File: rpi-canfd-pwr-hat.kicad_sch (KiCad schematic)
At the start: 72 parts, among them J1 Raspberry_Pi, J2 Conn_01x02, J3 Conn_01x02, J5 Conn_01x04_Pin, J6 Conn_01x02, U1 CAT24C256, U12 XC6206P332MR, U13 XC6206P182MR, U2 LM73100, U3 MCP2518FD, U4 TPS259472A, U5 TPS56637, U6 TCAN3413, U7 ICM-20948, Y1 48M

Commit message: schem: assign missing footprints
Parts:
- JP1: footprint (none) -> Jumper:SolderJumper-2_P1.3mm_Open_RoundedPad1.0x1.5mm
- JP2: footprint Jumper:SolderJumper-2_P1.3mm_Open_RoundedPad1.0x1.5mm -> Connector_PinHeader_2.54mm:PinHeader_1x02_P2.54mm_Horizontal
- U1: footprint (none) -> Package_SO:SOIC-8_3.9x4.9mm_P1.27mm
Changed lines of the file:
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@@
 			)
 		)
-		(property "Footprint" ""
+		(property "Footprint" "Jumper:SolderJumper-2_P1.3mm_Open_RoundedPad1.0x1.5mm"
 			(at 165.1 185.42 0)
 			(hide yes)
@@
 			)
 		)
-		(property "Footprint" "Jumper:SolderJumper-2_P1.3mm_Open_RoundedPad1.0x1.5mm"
+		(property "Footprint" "Connector_PinHeader_2.54mm:PinHeader_1x02_P2.54mm_Horizontal"
 			(at 266.7 127 0)
 			(hide yes)
@@
 			)
 		)
-		(property "Footprint" ""
+		(property "Footprint" "Package_SO:SOIC-8_3.9x4.9mm_P1.27mm"
 			(at 151.13 182.88 0)
 			(hide yes)

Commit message: schem: add ordering info to BOM
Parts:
- J1, J2, J3, J6, JP1, TP5, TP7, TP8: now left out of the parts list
- U1: Basic (none) -> X; JLCPCB Part # (none) -> C79987; Manufacturer (none) -> onsemi; Manufacturer Part Number (none) -> CAT24C256WI-GT3
- U12: Basic (none) -> Y; JLCPCB Part # (none) -> C5446; Manufacturer (none) -> Torex Semicon; Manufacturer Part Number (none) -> XC6206P332MR-G
- U13: Basic (none) -> X; JLCPCB Part # (none) -> C347373; Manufacturer (none) -> UMW; Manufacturer Part Number (none) -> XC6206P182MR
- U2: Basic (none) -> X; JLCPCB Part # (none) -> C3210761; Manufacturer (none) -> Texas Instruments; Manufacturer Part Number (none) -> LM73100RPWR
- U3: Basic (none) -> X; JLCPCB Part # (none) -> C621395; Manufacturer (none) -> Microchip Tech; Manufacturer Part Number (none) -> MCP2518FDT-E/QBB
- U6: Basic (none) -> X; JLCPCB Part # (none) -> C22433320; Manufacturer (none) -> Texas Instruments; Manufacturer Part Number (none) -> TCAN3413DR
- U7: Basic (none) -> X; JLCPCB Part # (none) -> C726001; Manufacturer (none) -> TDK InvenSense; Manufacturer Part Number (none) -> ICM-20948

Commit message: schem: add title
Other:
- company: (none) -> Rémi Ait-Younes
- title: (none) -> RPI CAN FD Power Hat+
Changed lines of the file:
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@@
 	(generator_version "10.0")
 	(paper "A4")
+	(title_block
+		(title "RPI CAN FD Power Hat+")
+		(date "2026-04-11")
+		(rev "01")
+		(company "Rémi Ait-Younes")
+	)
 	(rectangle
 		(start 191.77 25.4)

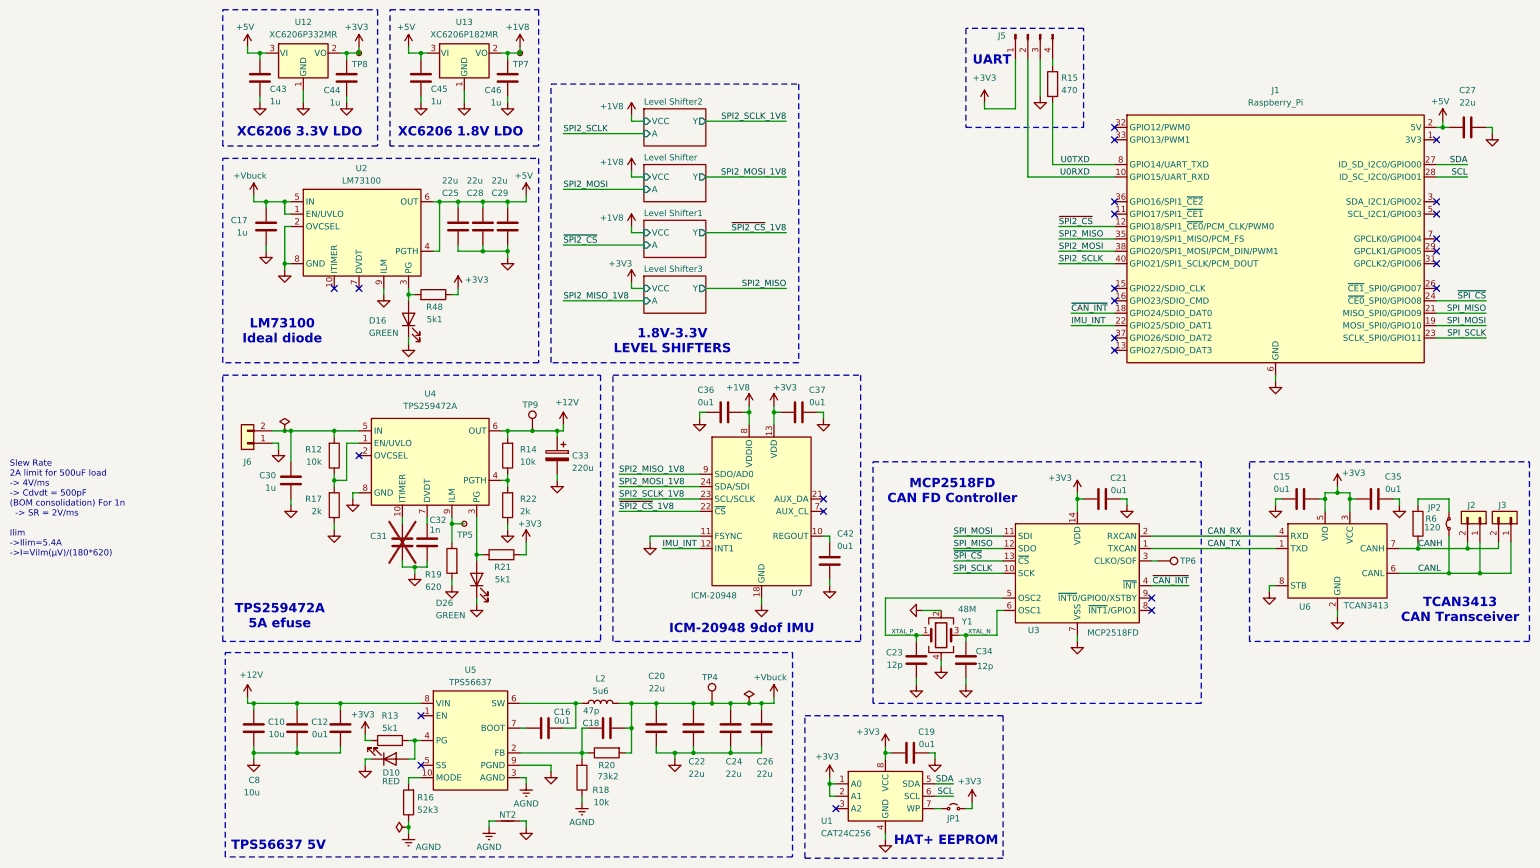
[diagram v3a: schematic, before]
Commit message: schem: renumber
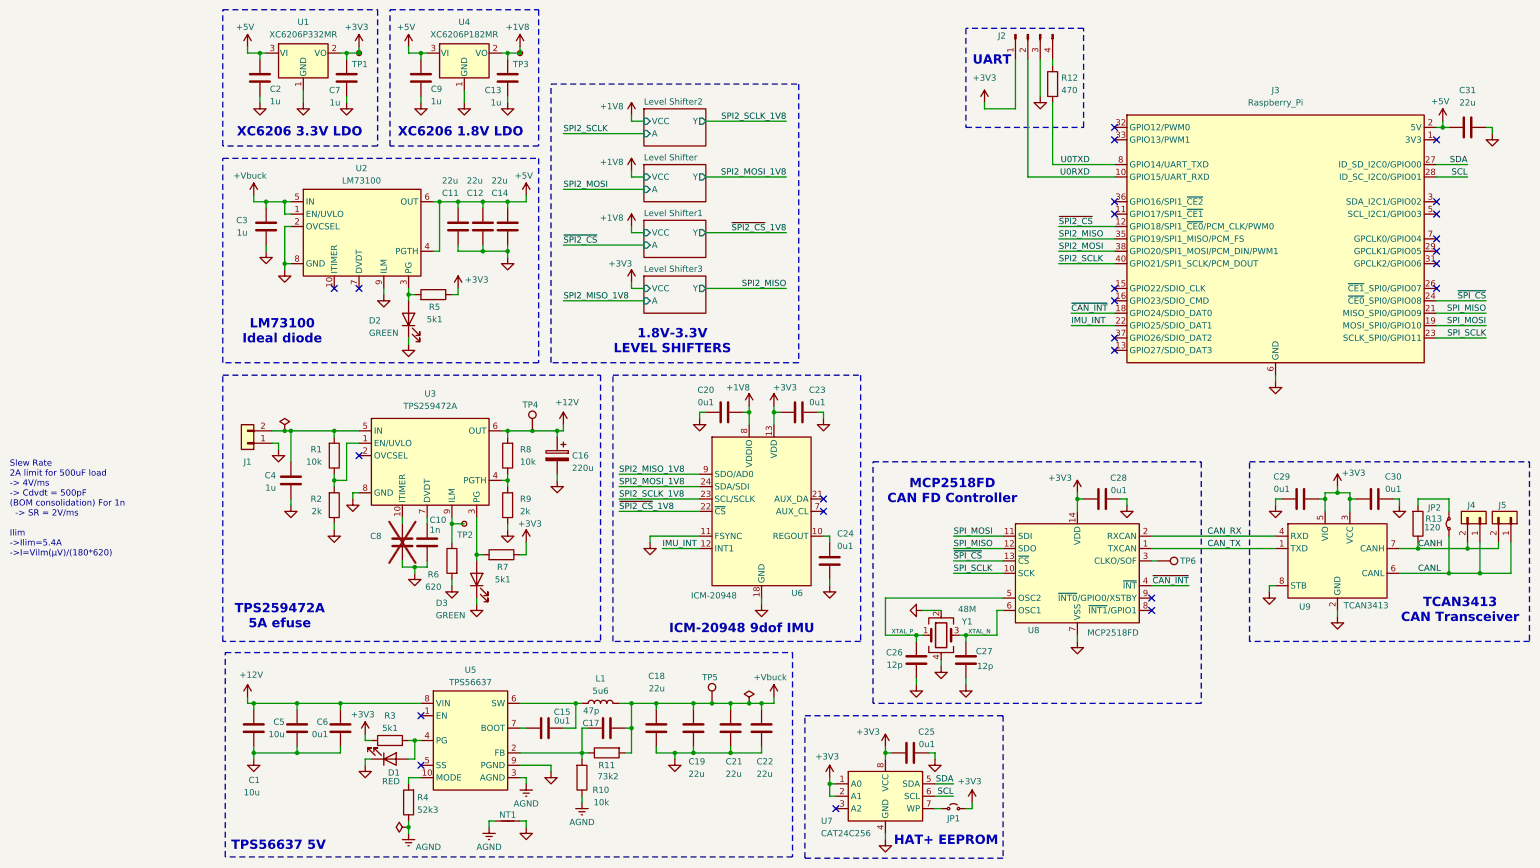
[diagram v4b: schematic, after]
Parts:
- renumbered C8 to C1, C32 to C10, C25 to C11, C28 to C12, C46 to C13, C29 to C14, C16 to C15, C33 to C16, C18 to C17, C20 to C18, C22 to C19, C43 to C2, C36 to C20, C24 to C21, C26 to C22, C37 to C23, C42 to C24, C19 to C25, C23 to C26, C34 to C27, C21 to C28, C15 to C29, C17 to C3, C35 to C30, C27 to C31, C30 to C4, C10 to C5, C12 to C6, C44 to C7, C31 to C8, C45 to C9, D10 to D1, D16 to D2, D26 to D3, J6 to J1, J5 to J2, J1 to J3, J2 to J4, J3 to J5, L2 to L1, NT2 to NT1, R12 to R1, R18 to R10, R20 to R11, R15 to R12, R6 to R13, R17 to R2, R13 to R3, R16 to R4, R48 to R5, R19 to R6, R21 to R7, R14 to R8, R22 to R9, TP8 to TP1, TP5 to TP2, TP7 to TP3, TP9 to TP4, TP4 to TP5, U12 to U1, U4 to U3, U13 to U4, U7 to U6, U1 to U7, U3 to U8, U6 to U9

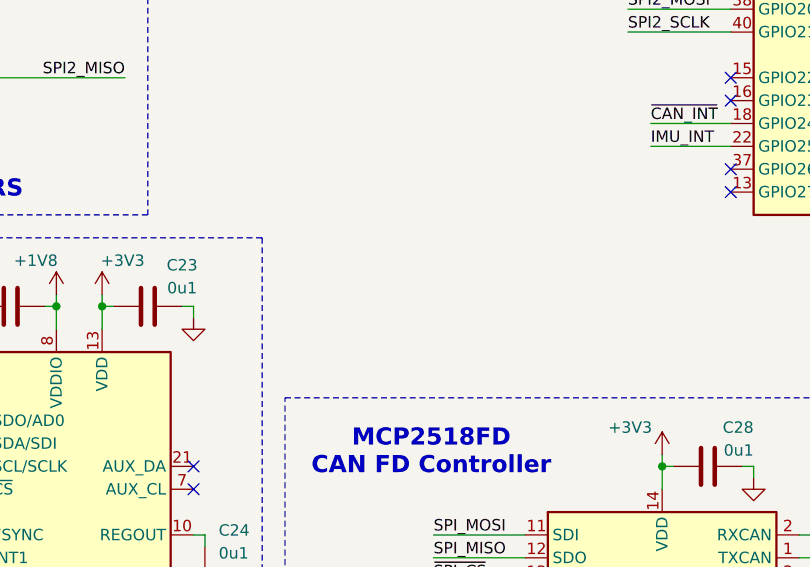
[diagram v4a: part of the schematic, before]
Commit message: schem: add smt fiducials and tooling holes
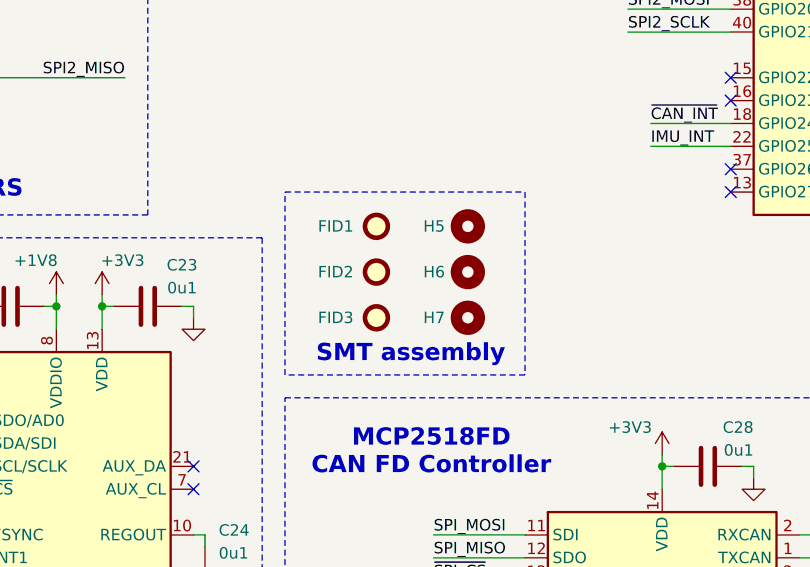
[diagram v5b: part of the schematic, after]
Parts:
- added FID1, FID2, FID3: Fiducial, Fiducial:Fiducial_1mm_Mask2mm, symbol Mechanical:Fiducial
- added H5, H6, H7: MountingHole, MountingHole:ToolingHole_1.152mm, symbol Mechanical:MountingHole
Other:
- note added: "SMT assembly"

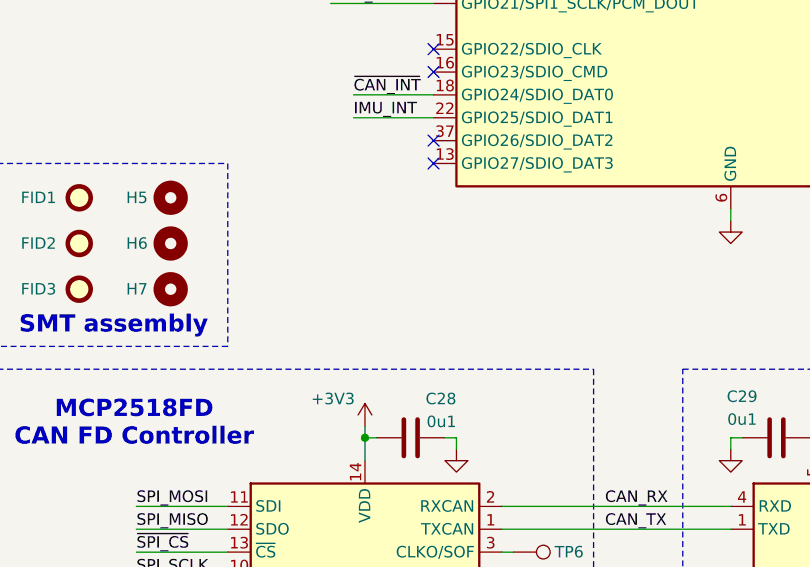
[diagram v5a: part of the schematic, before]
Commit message: schem: add hat mounting holes
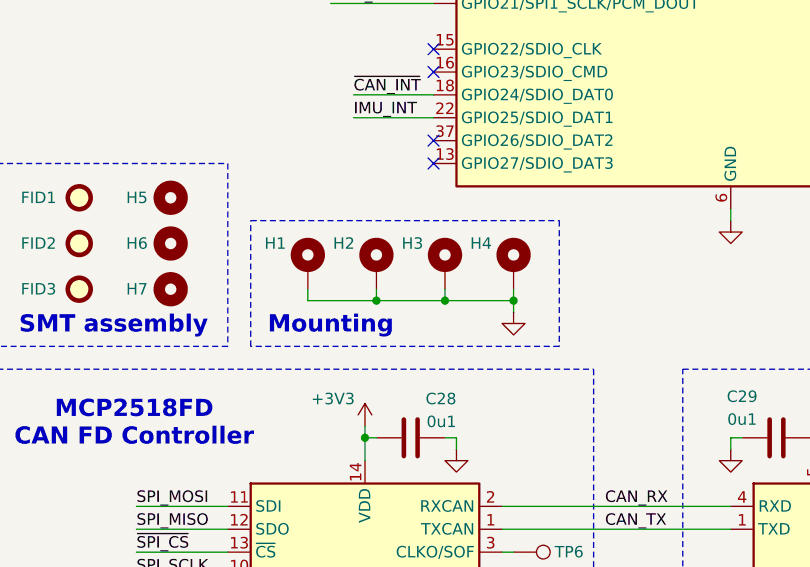
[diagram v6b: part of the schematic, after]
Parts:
- added H1, H2, H3, H4: MountingHole_Pad, MountingHole:MountingHole_2.7mm_M2.5_Pad_Via, symbol Mechanical:MountingHole_Pad
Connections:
- net GND: now also H1.1, H2.1, H3.1, H4.1
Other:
- note added: "Mounting"

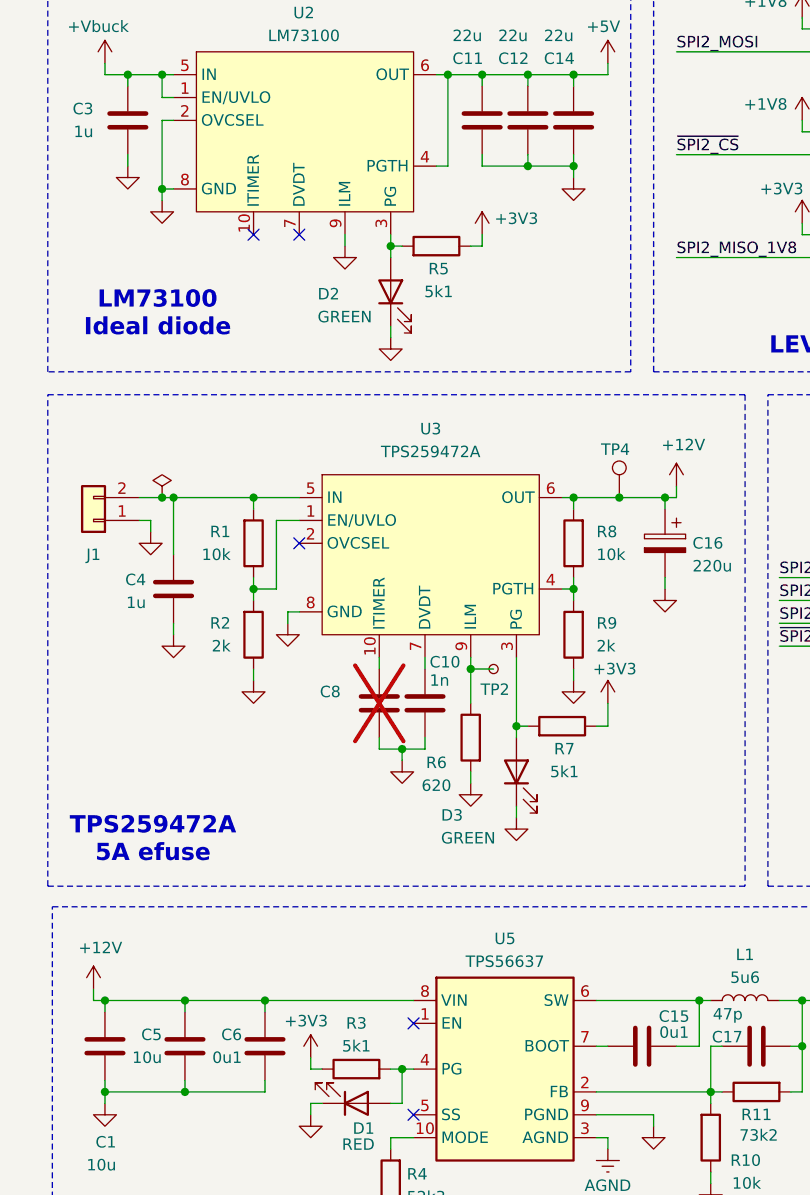
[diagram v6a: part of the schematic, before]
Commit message: pcb: add smps layout
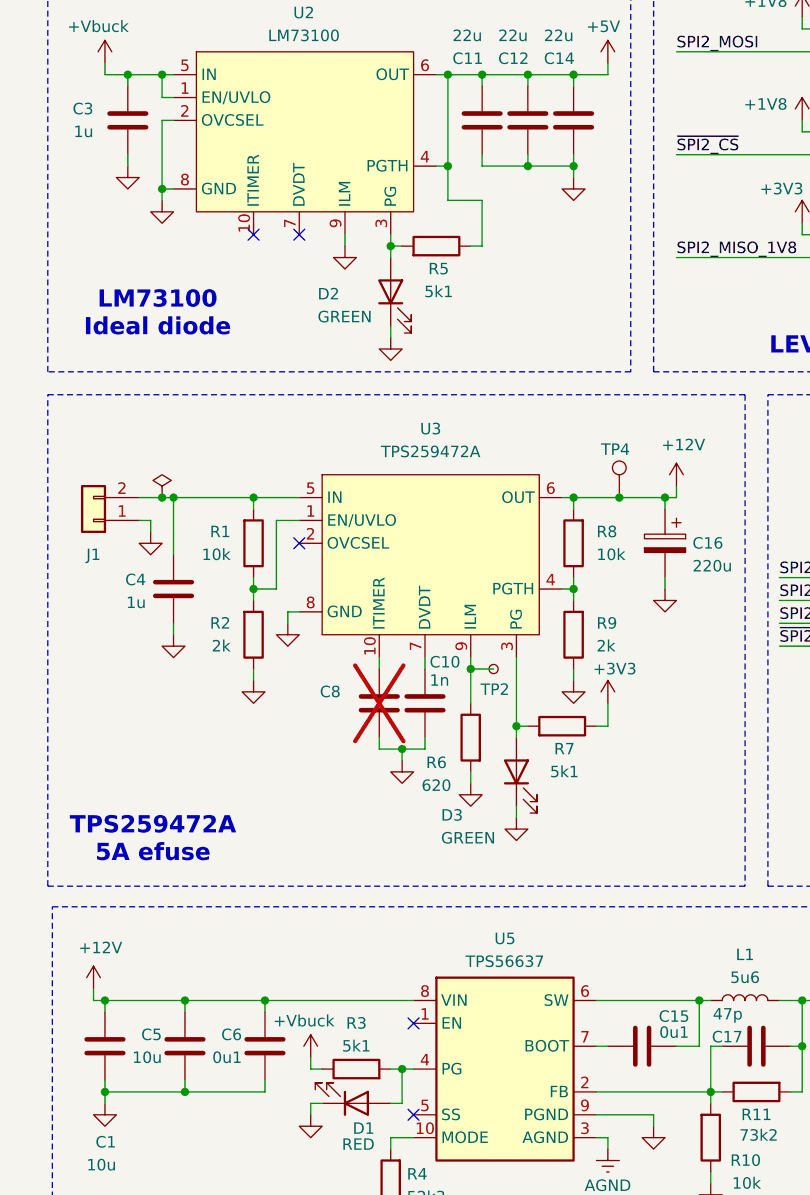
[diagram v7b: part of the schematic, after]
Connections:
- net +3V3: no longer R3.1, R5.1
- net +5V: now also R5.1
- net +Vbuck: now also R3.1
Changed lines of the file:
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@@
 	)
 	(junction
+		(at 59.69 71.12)
+		(diameter 0)
+		(color 0 0 0 0)
+	)
+	(junction
 		(at 24.13 60.96)
 		(diameter 0)
@@
 	(wire
 		(pts
+			(xy 63.5 74.93) (xy 59.69 74.93)
+		)
+		(stroke
+			(width 0)
+			(type default)
+		)
+	)
+	(wire
+		(pts
 			(xy 270.51 130.81) (xy 270.51 132.08)
 		)
@@
 	(wire
 		(pts
-			(xy 63.5 78.74) (xy 63.5 80.01)
+			(xy 63.5 74.93) (xy 63.5 80.01)
 		)
 		(stroke
@@
 	(wire
 		(pts
+			(xy 59.69 74.93) (xy 59.69 71.12)
+		)
+		(stroke
+			(width 0)
+			(type default)
+		)
+	)
+	(wire
+		(pts
 			(xy 85.09 69.85) (xy 101.6 69.85)
 		)
@@
 	)
 	(symbol
+		(lib_id "power:+12V")
+		(at 44.45 170.18 0)
+		(unit 1)
+		(body_style 1)
+		(exclude_from_sim no)
+		(in_bom yes)
+		(on_board yes)
+		(in_pos_files yes)
+		(dnp no)
+		(property "Reference" "#PWR087"
+			(at 44.45 173.99 0)
+			(hide yes)
+			(show_name no)
+			(do_not_autoplace no)
+			(effects
+				(font
+					(size 1.27 1.27)
+				)
+			)
+		)
+		(property "Value" "+Vbuck"
+			(at 43.688 166.116 0)
+			(show_name no)
+			(do_not_autoplace no)
+			(effects
+				(font
+					(size 1.27 1.27)
+				)
+			)
+		)
+		(property "Footprint" ""
+			(at 44.45 170.18 0)
+			(hide yes)
+			(show_name no)
+			(do_not_autoplace no)
+			(effects
+				(font
+					(size 1.27 1.27)
+				)
+			)
+		)
+		(property "Datasheet" ""
+			(at 44.45 170.18 0)
+			(hide yes)
+			(show_name no)
+			(do_not_autoplace no)
+			(effects
+				(font
+					(size 1.27 1.27)
+				)
+			)
+		)
+		(property "Description" "Power symbol creates a global label with name \"+12V\""
+			(at 44.45 170.18 0)
+			(hide yes)
+			(show_name no)
+			(do_not_autoplace no)
+			(effects
+				(font
+					(size 1.27 1.27)
+				)
+			)
+		)
+		(pin "1"
+		)
+		(instances
+			(project "rpi-canfd-pwr-hat"
+				(path "/35b6363d-fbe9-4c33-b2ab-05d20bd8dec5"
+					(reference "#PWR087")
+					(unit 1)
+				)
+			)
+		)
+	)
+	(symbol
 		(lib_id "power:GND")
 		(at 82.55 177.8 0)
@@
 	)
 	(symbol
-		(lib_id "power:+3V3")
-		(at 63.5 78.74 0)
-		(unit 1)
-		(body_style 1)
-		(exclude_from_sim no)
-		(in_bom yes)
-		(on_board yes)
-		(in_pos_files yes)
-		(dnp no)
-		(property "Reference" "#PWR024"
-			(at 63.5 82.55 0)
-			(hide yes)
-			(show_name no)
-			(do_not_autoplace no)
-			(effects
-				(font
-					(size 1.27 1.27)
-				)
-			)
-		)
-		(property "Value" "+3V3"
-			(at 67.31 76.962 0)
-			(show_name no)
-			(do_not_autoplace no)
-			(effects
-				(font
-					(size 1.27 1.27)
-				)
-			)
-		)
-		(property "Footprint" ""
-			(at 63.5 78.74 0)
-			(hide yes)
-			(show_name no)
-			(do_not_autoplace no)
-			(effects
-				(font
-					(size 1.27 1.27)
-				)
-			)
-		)
-		(property "Datasheet" ""
-			(at 63.5 78.74 0)
-			(hide yes)
-			(show_name no)
-			(do_not_autoplace no)
-			(effects
-				(font
-					(size 1.27 1.27)
-				)
-			)
-		)
-		(property "Description" "Power symbol creates a global label with name \"+3V3\""
-			(at 63.5 78.74 0)
-			(hide yes)
-			(show_name no)
-			(do_not_autoplace no)
-			(effects
-				(font
-					(size 1.27 1.27)
-				)
-			)
-		)
-		(pin "1"
-		)
-		(instances
-			(project "rpi-canfd-pwr-hat"
-				(path "/35b6363d-fbe9-4c33-b2ab-05d20bd8dec5"
-					(reference "#PWR024")
-					(unit 1)
-				)
-			)
-		)
-	)
-	(symbol
 		(lib_id "Interface_CAN_LIN:TCAN334")
 		(at 243.84 134.62 0)
@@
 					(unit 1)
 				)
-			)
-		)
-	)
-	(symbol
-		(lib_id "power:+3V3")
-		(at 44.45 170.18 0)
-		(unit 1)
-		(body_style 1)
-		(exclude_from_sim no)
-		(in_bom yes)
-		(on_board yes)
-		(in_pos_files yes)
-		(dnp no)
-		(fields_autoplaced yes)
-		(property "Reference" "#PWR015"
-			(at 44.45 173.99 0)
-			(hide yes)
-			(show_name no)
-			(do_not_autoplace no)
-			(effects
-				(font
-					(size 1.27 1.27)
-				)
-			)
-		)
-		(property "Value" "+3V3"
-			(at 43.942 166.116 0)
-			(show_name no)
-			(do_not_autoplace no)
-			(effects
-				(font
-					(size 1.27 1.27)
-				)
-			)
-		)
-		(property "Footprint" ""
-			(at 44.45 170.18 0)
-			(hide yes)
-			(show_name no)
-			(do_not_autoplace no)
-			(effects
-				(font
-					(size 1.27 1.27)
-				)
-			)
-		)
-		(property "Datasheet" ""
-			(at 44.45 170.18 0)
-			(hide yes)
-			(show_name no)
-			(do_not_autoplace no)
-			(effects
-				(font
-					(size 1.27 1.27)
-				)
-			)
-		)
-		(property "Description" "Power symbol creates a global label with name \"+3V3\""
-			(at 44.45 170.18 0)
-			(hide yes)
-			(show_name no)
-			(do_not_autoplace no)
-			(effects
-				(font
-					(size 1.27 1.27)
-				)
-			)
-		)
-		(pin "1"
-		)
-		(instances
-			(project "rpi-canfd-pwr-hat"
-				(path "/35b6363d-fbe9-4c33-b2ab-05d20bd8dec5"
-					(reference "#PWR015")
-					(unit 1)
-				)
